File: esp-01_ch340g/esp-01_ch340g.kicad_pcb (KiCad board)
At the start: 2 copper layers, 25.4 x 32.4 mm, 7 parts, among them SW1 Flash, SW2 Reset, SW3 Flash2, SW4 Reset2, U1 ESP-01

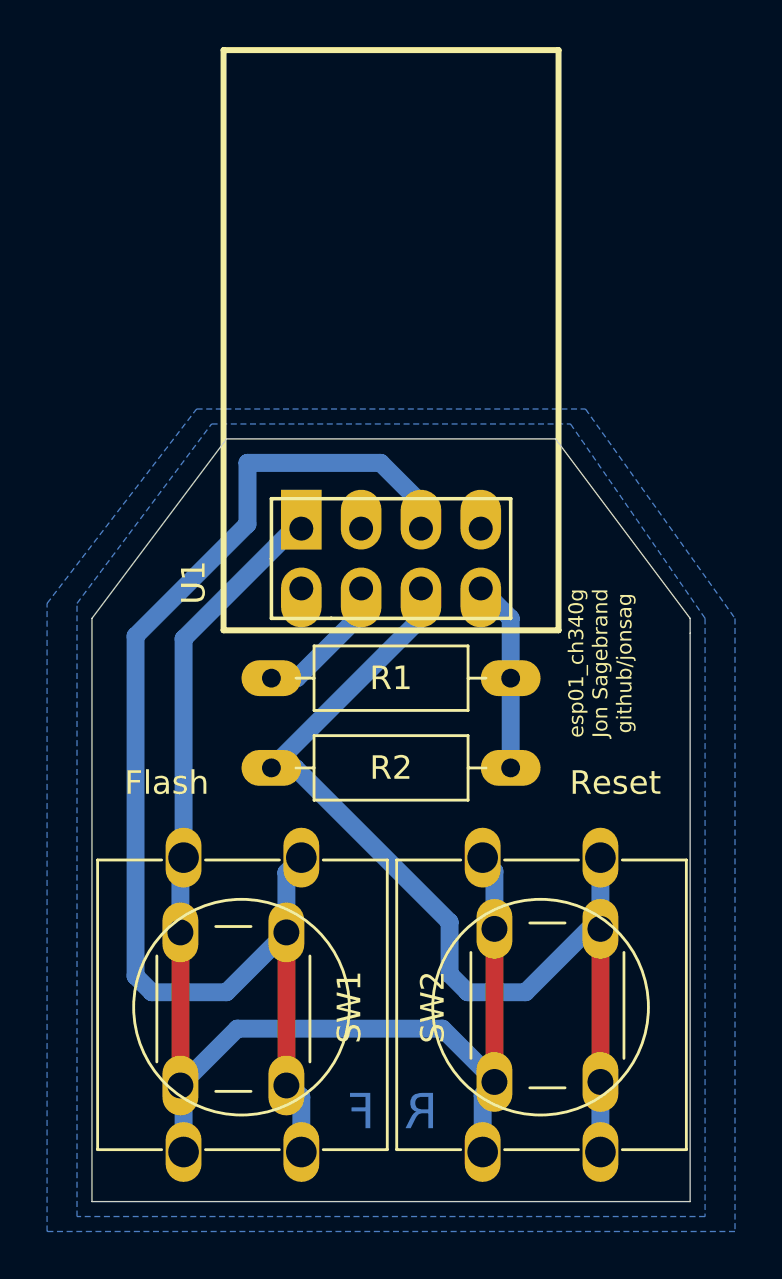
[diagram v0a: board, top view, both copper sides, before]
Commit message: esp-01 programmer board
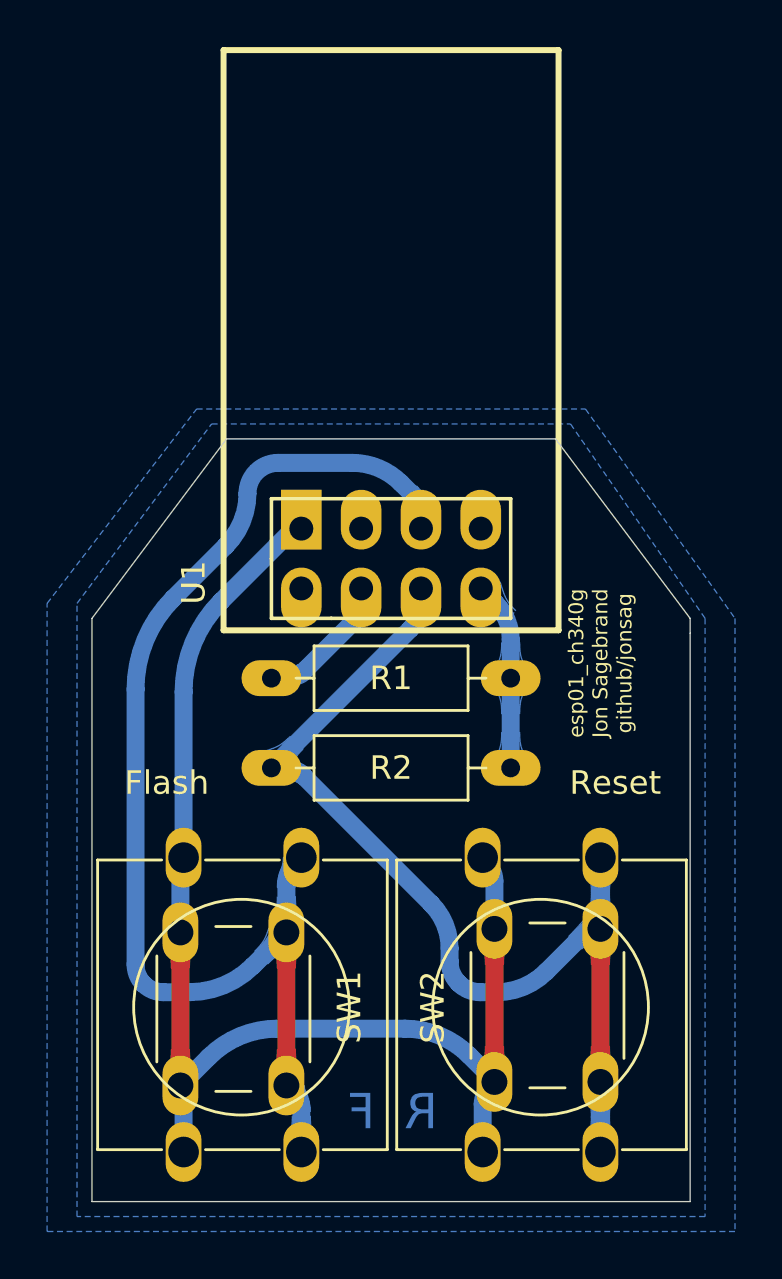
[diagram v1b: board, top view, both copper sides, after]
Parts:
- SW1: value Flash -> Flash 12mm
- SW2: value Reset -> Reset 12mm
- SW3: value Flash2 -> Flash 6mm
- SW4: value Reset2 -> Reset 6mm
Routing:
- net Net-(SW3-Pad1): track 53.7 -> 51.9 mm
- net Net-(R2-Pad2): track 43.3 -> 42.2 mm
- net GND: track 57.1 -> 56.2 mm
